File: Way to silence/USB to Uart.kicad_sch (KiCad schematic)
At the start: 2 parts, among them U3 CP2102-GMR, U5 USB-TYPE-C-018

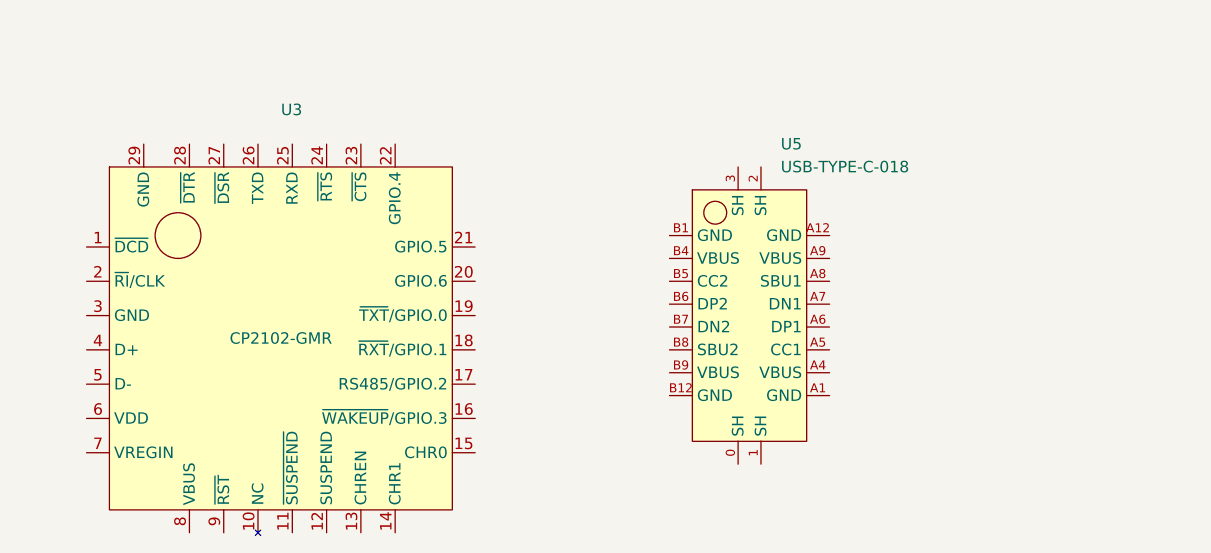
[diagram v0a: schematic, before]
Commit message: [ADD] USB C Connections
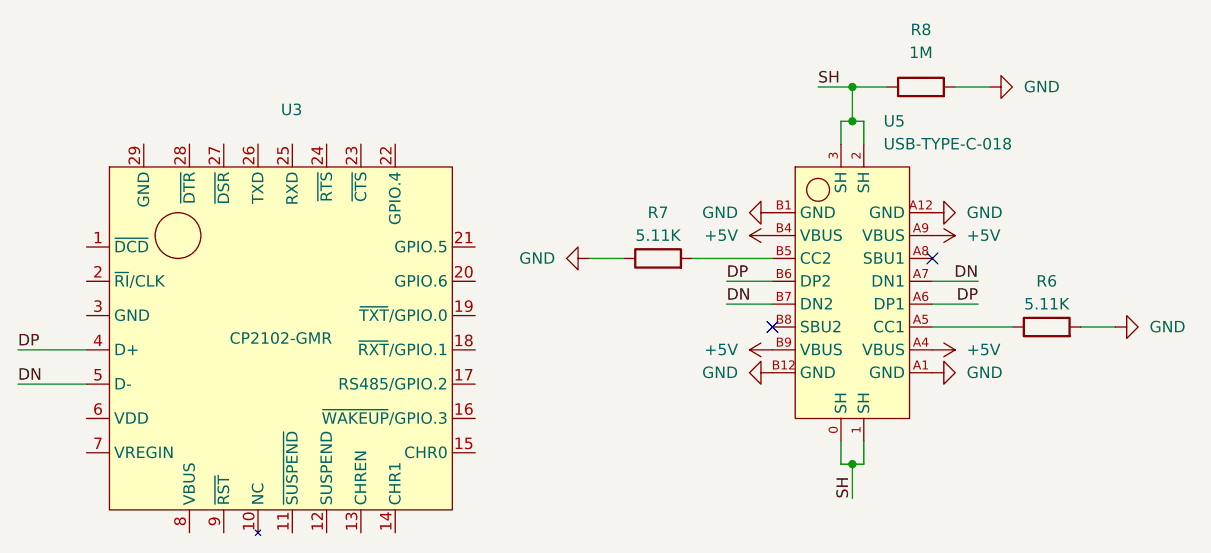
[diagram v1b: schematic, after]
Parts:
- added R6, R7: 5.11K, symbol Way to silence:R
- added R8: 1M, symbol Way to silence:R
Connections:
- net DP: now reaches U3.4 (D+)
- net DP: now also U5.A6 (DP1), U5.B6 (DP2)
- net DN: now reaches U3.5 (D-)
- net DN: now also U5.A7 (DN1), U5.B7 (DN2)
- net SH: now reaches U5.0 (SH)
- net SH: now also U5.1 (SH), U5.2 (SH), U5.3 (SH), R8.1
- net GND: now reaches U5.A1 (GND)
- net GND: now also U5.A12 (GND), U5.B1 (GND), U5.B12 (GND), R6.2, R7.1, R8.2
- net +5V: now reaches U5.A4 (VBUS)
- net +5V: now also U5.A9 (VBUS), U5.B4 (VBUS), U5.B9 (VBUS)
- net at U5.A5 (CC1): now also R6.1
- net at U5.B5 (CC2): now also R7.2
- no-connect marks 0 -> 2
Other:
- moved on the sheet: U5

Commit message: [DRC] Working on USB to UART Sheet
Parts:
- added C2, C3: 100nF, symbol Way to silence:C
- added C4: 4.7uF, symbol Way to silence:C
- added Q1, Q2: BC817, Package_TO_SOT_SMD:SOT-23, symbol Way to silence:BC817
- added R10, R9: 10K, symbol Way to silence:R
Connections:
- net +5V: now also U3.7 (VREGIN), U3.8 (VBUS), C3.2, C4.2
- net GND: now also U3.29 (GND), U3.3 (GND), C2.1, C3.1, C4.1
- net at U3.24 (~{RTS}): now also Q2.2 (E), R9.1
- net RXD: now reaches U3.25 (RXD)
- net TXD: now reaches U3.26 (TXD)
- net at U3.28 (~{DTR}): now also Q1.2 (E), R10.1
- net at U3.6 (VDD): now also C2.2
- new net: Q2.1 (B), R10.2
- new net: Q1.1 (B), R9.2
- new net EN: Q2.3 (C)
- new net IO0: Q1.3 (C)
- no-connect marks 2 -> 19
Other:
- moved on the sheet: U3

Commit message: [ADD] Completed some connections in main sheet
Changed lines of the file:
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@@
+    (stroke (width 0) (type default))
+  )
+  (wire (pts (xy 25.4 27.94) (xy 35.56 27.94))
     (stroke (width 0) (type default))
   )
@@
     (effects (font (size 1.27 1.27)) (justify right bottom))
   )
+  (label "USB +5V" (at 162.56 45.72 180) (fields_autoplaced)
+    (effects (font (size 1.27 1.27)) (justify right bottom))
+  )
+  (label "USB +5V" (at 180.34 58.42 0) (fields_autoplaced)
+    (effects (font (size 1.27 1.27)) (justify left bottom))
+  )
+  (label "USB +5V" (at 162.56 58.42 180) (fields_autoplaced)
+    (effects (font (size 1.27 1.27)) (justify right bottom))
+  )
+  (label "USB +5V" (at 35.56 27.94 0) (fields_autoplaced)
+    (effects (font (size 1.27 1.27)) (justify left bottom))
+  )
+  (label "USB +5V" (at 180.34 45.72 0) (fields_autoplaced)
+    (effects (font (size 1.27 1.27)) (justify left bottom))
+  )
   (label "DP" (at 157.48 50.8 0) (fields_autoplaced)
     (effects (font (size 1.27 1.27)) (justify left bottom))
@@
   (label "DN" (at 80.01 83.82 0) (fields_autoplaced)
     (effects (font (size 1.27 1.27)) (justify left bottom))
+  )
+  (label "USB +5V" (at 54.61 91.44 180) (fields_autoplaced)
+    (effects (font (size 1.27 1.27)) (justify right bottom))
   )
   (label "DN" (at 185.42 50.8 180) (fields_autoplaced)
@@
     (effects (font (size 1.27 1.27)) (justify right))
   )
-  (symbol (lib_id "power:+5V") (at 162.56 58.42 90) (unit 1)
-    (in_bom yes) (on_board yes) (dnp no) (fields_autoplaced)
-    (property "Reference" "#PWR012" (at 166.37 58.42 0)
-      (effects (font (size 1.27 1.27)) hide)
-    )
-    (property "Value" "+5V" (at 158.75 58.42 90)
-      (effects (font (size 1.27 1.27)) (justify left))
-    )
-    (property "Footprint" "" (at 162.56 58.42 0)
-      (effects (font (size 1.27 1.27)) hide)
-    )
-    (property "Datasheet" "" (at 162.56 58.42 0)
-      (effects (font (size 1.27 1.27)) hide)
-    )
-    (pin "1")
-    (instances
-      (project "Way to silence"
-        (path "/9822a1be-a034-44c3-8530-56368958b215/a2ee35dd-b0f9-4eed-a2dd-4bc114f32cf5"
-          (reference "#PWR012") (unit 1)
-        )
-      )
-    )
+  (hierarchical_label "+5V" (shape input) (at 25.4 27.94 180) (fields_autoplaced)
+    (effects (font (size 1.27 1.27)) (justify right))
   )
   (symbol (lib_id "power:GND") (at 142.24 48.26 270) (unit 1)
@@
     )
     (property "Value" "GND" (at 140.97 58.42 90)
-      (effects (font (size 1.27 1.27)) (justify right))
+      (effects (font (size 1.27 1.27)) (justify right) hide)
     )
     (property "Footprint" "" (at 142.24 48.26 0)
@@
         (path "/9822a1be-a034-44c3-8530-56368958b215/a2ee35dd-b0f9-4eed-a2dd-4bc114f32cf5"
           (reference "R8") (unit 1)
-        )
-      )
-    )
-  )
-  (symbol (lib_id "power:+5V") (at 180.34 58.42 270) (unit 1)
-    (in_bom yes) (on_board yes) (dnp no) (fields_autoplaced)
-    (property "Reference" "#PWR013" (at 176.53 58.42 0)
-      (effects (font (size 1.27 1.27)) hide)
-    )
-    (property "Value" "+5V" (at 184.15 58.42 90)
-      (effects (font (size 1.27 1.27)) (justify left))
-    )
-    (property "Footprint" "" (at 180.34 58.42 0)
-      (effects (font (size 1.27 1.27)) hide)
-    )
-    (property "Datasheet" "" (at 180.34 58.42 0)
-      (effects (font (size 1.27 1.27)) hide)
-    )
-    (pin "1")
-    (instances
-      (project "Way to silence"
-        (path "/9822a1be-a034-44c3-8530-56368958b215/a2ee35dd-b0f9-4eed-a2dd-4bc114f32cf5"
-          (reference "#PWR013") (unit 1)
-        )
-      )
-    )
-  )
-  (symbol (lib_id "power:+5V") (at 180.34 45.72 270) (unit 1)
-    (in_bom yes) (on_board yes) (dnp no) (fields_autoplaced)
-    (property "Reference" "#PWR06" (at 176.53 45.72 0)
-      (effects (font (size 1.27 1.27)) hide)
-    )
-    (property "Value" "+5V" (at 184.15 45.72 90)
-      (effects (font (size 1.27 1.27)) (justify left))
-    )
-    (property "Footprint" "" (at 180.34 45.72 0)
-      (effects (font (size 1.27 1.27)) hide)
-    )
-    (property "Datasheet" "" (at 180.34 45.72 0)
-      (effects (font (size 1.27 1.27)) hide)
-    )
-    (pin "1")
-    (instances
-      (project "Way to silence"
-        (path "/9822a1be-a034-44c3-8530-56368958b215/a2ee35dd-b0f9-4eed-a2dd-4bc114f32cf5"
-          (reference "#PWR06") (unit 1)
         )
       )
@@
         (path "/9822a1be-a034-44c3-8530-56368958b215/a2ee35dd-b0f9-4eed-a2dd-4bc114f32cf5"
           (reference "R6") (unit 1)
-        )
-      )
-    )
-  )
-  (symbol (lib_id "power:+5V") (at 162.56 45.72 90) (unit 1)
-    (in_bom yes) (on_board yes) (dnp no) (fields_autoplaced)
-    (property "Reference" "#PWR011" (at 166.37 45.72 0)
-      (effects (font (size 1.27 1.27)) hide)
-    )
-    (property "Value" "+5V" (at 158.75 45.72 90)
-      (effects (font (size 1.27 1.27)) (justify left))
-    )
-    (property "Footprint" "" (at 162.56 45.72 0)
-      (effects (font (size 1.27 1.27)) hide)
-    )
-    (property "Datasheet" "" (at 162.56 45.72 0)
-      (effects (font (size 1.27 1.27)) hide)
-    )
-    (pin "1")
-    (instances
-      (project "Way to silence"
-        (path "/9822a1be-a034-44c3-8530-56368958b215/a2ee35dd-b0f9-4eed-a2dd-4bc114f32cf5"
-          (reference "#PWR011") (unit 1)
         )
       )
@@
         )
       )
-    )
-  )
-  (symbol (lib_id "power:+5V") (at 54.61 91.44 90) (unit 1)
-    (in_bom yes) (on_board yes) (dnp no) (fields_autoplaced)
-    (property "Reference" "#PWR024" (at 58.42 91.44 0)
-      (effects (font (size 1.27 1.27)) hide)
-    )
-    (property "Value" "+5V" (at 50.8 91.44 90)
-      (effects (font (size 1.27 1.27)) (justify left))
-    )
-    (property "Footprint" "" (at 54.61 91.44 0)
-      (effects (font (size 1.27 1.27)) hide)
-    )
-    (property "Datasheet" "" (at 54.61 91.44 0)
-      (effects (font (size 1.27 1.27)) hide)
-    )
-    (pin "1")
-    (instances
-      (project "Way to silence"
-        (path "/9822a1be-a034-44c3-8530-56368958b215/a2ee35dd-b0f9-4eed-a2dd-4bc114f32cf5"
-          (reference "#PWR024") (unit 1)
-        )
-      )

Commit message: [ADD] 3v3 Reg
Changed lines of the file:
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@@
   (junction (at 87.63 91.44) (diameter 0) (color 0 0 0 0)
+  )
+  (junction (at 87.63 101.6) (diameter 0) (color 0 0 0 0)
   )
   (junction (at 73.66 87.63) (diameter 0) (color 0 0 0 0)
@@
         )
       )
+    )
+  )
+  (symbol (lib_id "power:PWR_FLAG") (at 87.63 101.6 180) (unit 1)
+    (in_bom yes) (on_board yes) (dnp no) (fields_autoplaced)
+    (property "Reference" "#FLG06" (at 87.63 103.505 0)
+      (effects (font (size 1.27 1.27)) hide)
+    )
+    (property "Value" "PWR_FLAG" (at 87.63 106.68 0)
+      (effects (font (size 1.27 1.27)))
+    )
+    (property "Footprint" "" (at 87.63 101.6 0)
+      (effects (font (size 1.27 1.27)) hide)
+    )
+    (property "Datasheet" "~" (at 87.63 101.6 0)
+      (effects (font (size 1.27 1.27)) hide)
+    )
+    (pin "1")
+    (instances
+      (project "Way to silence"
+        (path "/9822a1be-a034-44c3-8530-56368958b215/a2ee35dd-b0f9-4eed-a2dd-4bc114f32cf5"
+          (reference "#FLG06") (unit 1)
+        )
+      )

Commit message: [ADD] New reg footprint and datasheet
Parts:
- Q1, Q2: LCSC (none) -> C475629
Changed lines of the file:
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@@
       (effects (font (size 1.27 1.27)) (justify left) hide)
+    )
+    (property "LCSC" "C475629" (at 64.77 22.86 0)
+      (effects (font (size 1.27 1.27)) hide)
     )
     (pin "1")
@@
       (effects (font (size 1.27 1.27)) (justify left) hide)
     )
-    (pin "1")
+    (property "LCSC" "C475629" (at 64.77 38.1 0)
+      (effects (font (size 1.27 1.27)) hide)
+    )
+    (pin "1")

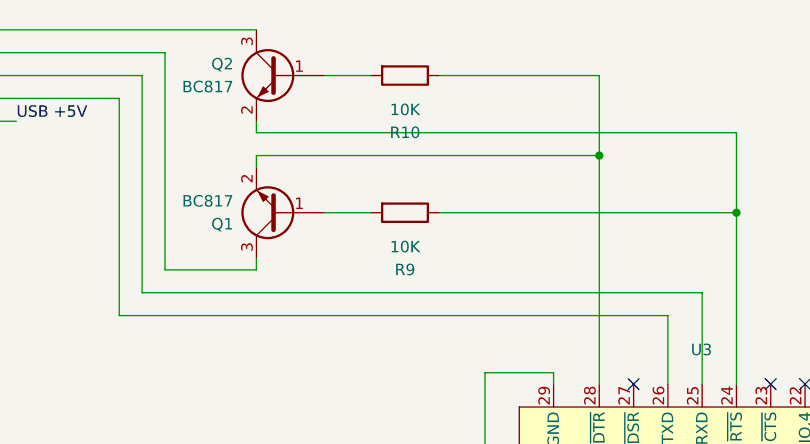
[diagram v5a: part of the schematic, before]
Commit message: [ADD] LSCS Parts and Footprints for BMS
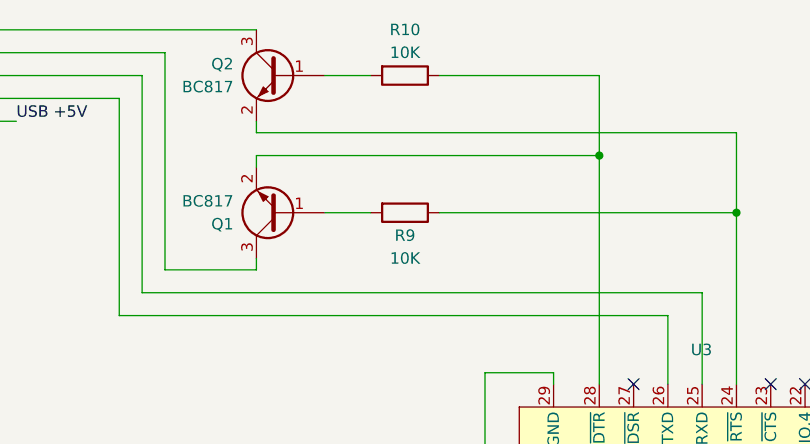
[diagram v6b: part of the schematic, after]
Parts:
- C2, C3, C4: footprint (none) -> Way to silence:C_0603_1608Metric
- R10, R6, R7, R8, R9: footprint (none) -> Way to silence:R_0603_1608Metric
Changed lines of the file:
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@@
       (effects (font (size 1.27 1.27)))
     )
-    (property "Footprint" "" (at 179.07 30.988 0)
+    (property "Footprint" "Way to silence:R_0603_1608Metric" (at 179.07 30.988 0)
       (effects (font (size 1.27 1.27)) hide)
     )
@@
   )
   (symbol (lib_id "Way to silence:R") (at 78.74 22.86 180) (unit 1)
-    (in_bom yes) (on_board yes) (dnp no) (fields_autoplaced)
-    (property "Reference" "R10" (at 78.74 29.21 0)
-      (effects (font (size 1.27 1.27)))
-    )
-    (property "Value" "10K" (at 78.74 26.67 0)
-      (effects (font (size 1.27 1.27)))
-    )
-    (property "Footprint" "" (at 78.74 21.082 0)
+    (in_bom yes) (on_board yes) (dnp no)
+    (property "Reference" "R10" (at 78.74 17.78 0)
+      (effects (font (size 1.27 1.27)))
+    )
+    (property "Value" "10K" (at 78.74 20.32 0)
+      (effects (font (size 1.27 1.27)))
+    )
+    (property "Footprint" "Way to silence:R_0603_1608Metric" (at 78.74 21.082 0)
       (effects (font (size 1.27 1.27)) hide)
     )
@@
       (effects (font (size 1.27 1.27)))
     )
-    (property "Footprint" "" (at 193.04 57.658 0)
+    (property "Footprint" "Way to silence:R_0603_1608Metric" (at 193.04 57.658 0)
       (effects (font (size 1.27 1.27)) hide)
     )
@@
       (effects (font (size 1.27 1.27)) (justify right))
     )
-    (property "Footprint" "" (at 73.9648 91.44 90)
+    (property "Footprint" "Way to silence:C_0603_1608Metric" (at 73.9648 91.44 90)
       (effects (font (size 1.27 1.27)) hide)
     )
@@
       (effects (font (size 1.27 1.27)) (justify right))
     )
-    (property "Footprint" "" (at 59.9948 91.44 90)
+    (property "Footprint" "Way to silence:C_0603_1608Metric" (at 59.9948 91.44 90)
       (effects (font (size 1.27 1.27)) hide)
     )
@@
       (effects (font (size 1.27 1.27)))
     )
-    (property "Footprint" "" (at 149.86 50.038 0)
+    (property "Footprint" "Way to silence:R_0603_1608Metric" (at 149.86 50.038 0)
       (effects (font (size 1.27 1.27)) hide)
     )
@@
   )
   (symbol (lib_id "Way to silence:R") (at 78.74 38.1 180) (unit 1)
-    (in_bom yes) (on_board yes) (dnp no) (fields_autoplaced)
-    (property "Reference" "R9" (at 78.74 44.45 0)
-      (effects (font (size 1.27 1.27)))
-    )
-    (property "Value" "10K" (at 78.74 41.91 0)
-      (effects (font (size 1.27 1.27)))
-    )
-    (property "Footprint" "" (at 78.74 36.322 0)
+    (in_bom yes) (on_board yes) (dnp no)
+    (property "Reference" "R9" (at 78.74 40.64 0)
+      (effects (font (size 1.27 1.27)))
+    )
+    (property "Value" "10K" (at 78.74 43.18 0)
+      (effects (font (size 1.27 1.27)))
+    )
+    (property "Footprint" "Way to silence:R_0603_1608Metric" (at 78.74 36.322 0)
       (effects (font (size 1.27 1.27)) hide)
     )
@@
       (effects (font (size 1.27 1.27)))
     )
-    (property "Footprint" "" (at 67.31 86.6648 90)
-      (effects (font (size 1.27 1.27)) hide)
-    )
+    (property "Footprint" "Way to silence:C_0603_1608Metric" (at 67.31 86.6648 90)
+      (effects (font (size 1.27 1.27)) hide)
+    )

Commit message: [ADD] LCSC References
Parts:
- C2, C3: LSCS (none) -> C14663
- C4: LSCS (none) -> C19666
- R10, R9: LSCS (none) -> C25804
- R6, R7: LSCS (none) -> C425414
- R8: LSCS (none) -> C22935
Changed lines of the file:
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@@
+      (effects (font (size 1.27 1.27)) hide)
+    )
+    (property "LSCS" "C22935" (at 179.07 29.21 0)
       (effects (font (size 1.27 1.27)) hide)
     )
@@
       (effects (font (size 1.27 1.27)) hide)
     )
+    (property "LSCS" "C25804" (at 78.74 22.86 0)
+      (effects (font (size 1.27 1.27)) hide)
+    )
     (pin "1")
     (pin "2")
@@
     )
     (property "Datasheet" "~" (at 193.04 55.88 90)
+      (effects (font (size 1.27 1.27)) hide)
+    )
+    (property "LSCS" "C425414" (at 193.04 55.88 0)
       (effects (font (size 1.27 1.27)) hide)
     )
@@
       (effects (font (size 1.27 1.27)) hide)
     )
+    (property "LSCS" "C19666" (at 74.93 95.25 90)
+      (effects (font (size 1.27 1.27)) hide)
+    )
     (pin "1")
     (pin "2")
@@
     )
     (property "Datasheet" "~" (at 60.96 95.25 90)
+      (effects (font (size 1.27 1.27)) hide)
+    )
+    (property "LSCS" "C14663" (at 60.96 95.25 90)
       (effects (font (size 1.27 1.27)) hide)
     )
@@
       (effects (font (size 1.27 1.27)) hide)
     )
+    (property "LSCS" "C425414" (at 149.86 48.26 0)
+      (effects (font (size 1.27 1.27)) hide)
+    )
     (pin "1")
     (pin "2")
@@
       (effects (font (size 1.27 1.27)) hide)
     )
+    (property "LSCS" "C25804" (at 78.74 38.1 0)
+      (effects (font (size 1.27 1.27)) hide)
+    )
     (pin "1")
     (pin "2")
@@
       (effects (font (size 1.27 1.27)) hide)
     )
+    (property "LSCS" "C14663" (at 63.5 87.63 0)
+      (effects (font (size 1.27 1.27)) hide)
+    )

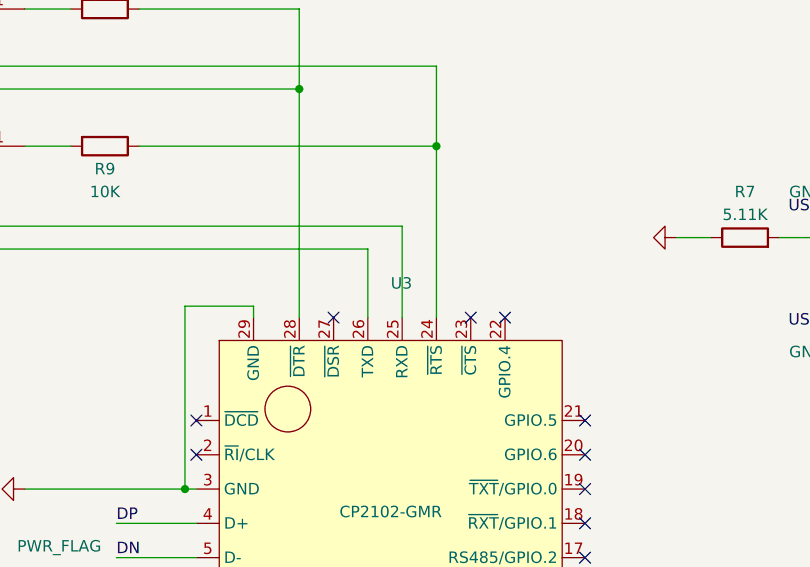
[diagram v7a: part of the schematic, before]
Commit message: [ADD] Styles to shematics
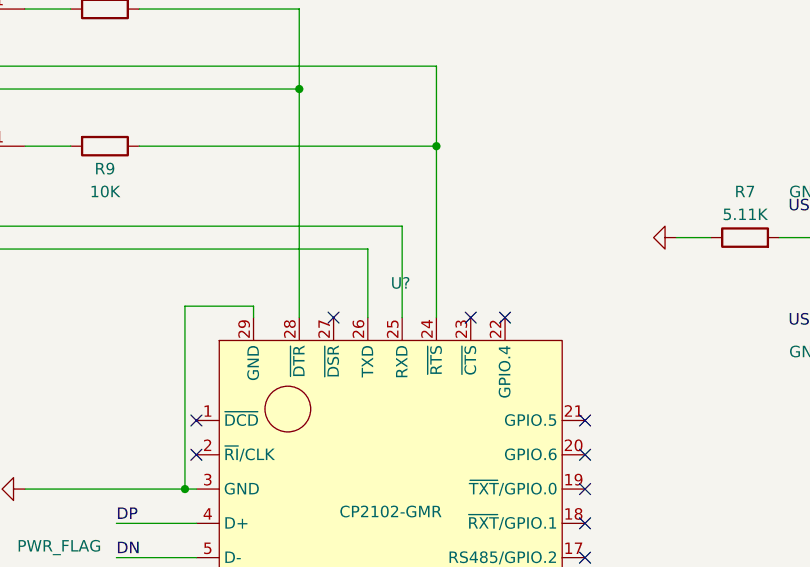
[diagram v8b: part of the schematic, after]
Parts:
- renumbered U3 to U?
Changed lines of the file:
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@@
   (symbol (lib_id "Way to silence:CP2102") (at 110.49 78.74 0) (unit 1)
     (in_bom yes) (on_board yes) (dnp no)
-    (property "Reference" "U3" (at 110.49 53.34 0)
+    (property "Reference" "U?" (at 110.49 53.34 0)
       (effects (font (size 1.27 1.27)) (justify left))
     )
@@
       (project "Way to silence"
         (path "/9822a1be-a034-44c3-8530-56368958b215"
-          (reference "U3") (unit 1)
+          (reference "U?") (unit 1)
         )
         (path "/9822a1be-a034-44c3-8530-56368958b215/a2ee35dd-b0f9-4eed-a2dd-4bc114f32cf5"
